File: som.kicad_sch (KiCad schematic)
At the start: 31 parts, among them M1 jetson-orin-nx/nano-module, U4 NTS0102GT

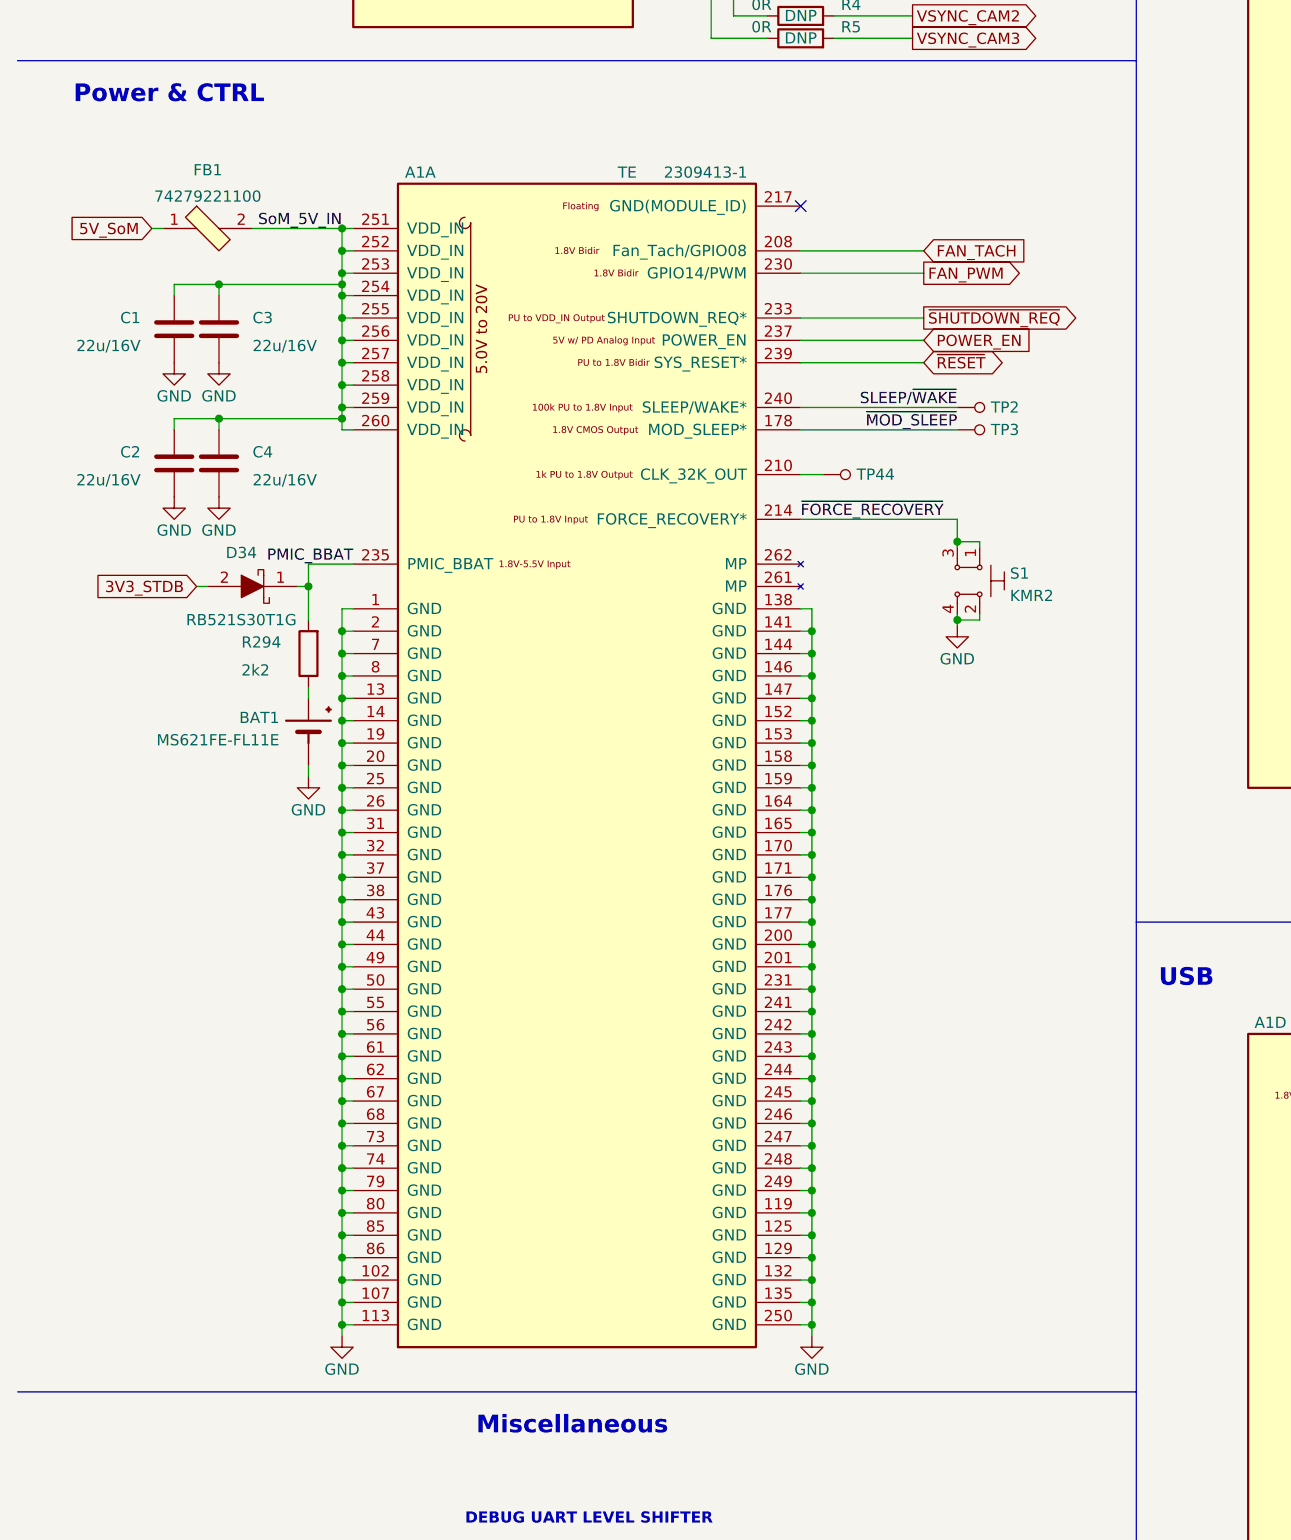
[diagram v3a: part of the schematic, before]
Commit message: Add more capacitors to the SoM VDD_IN
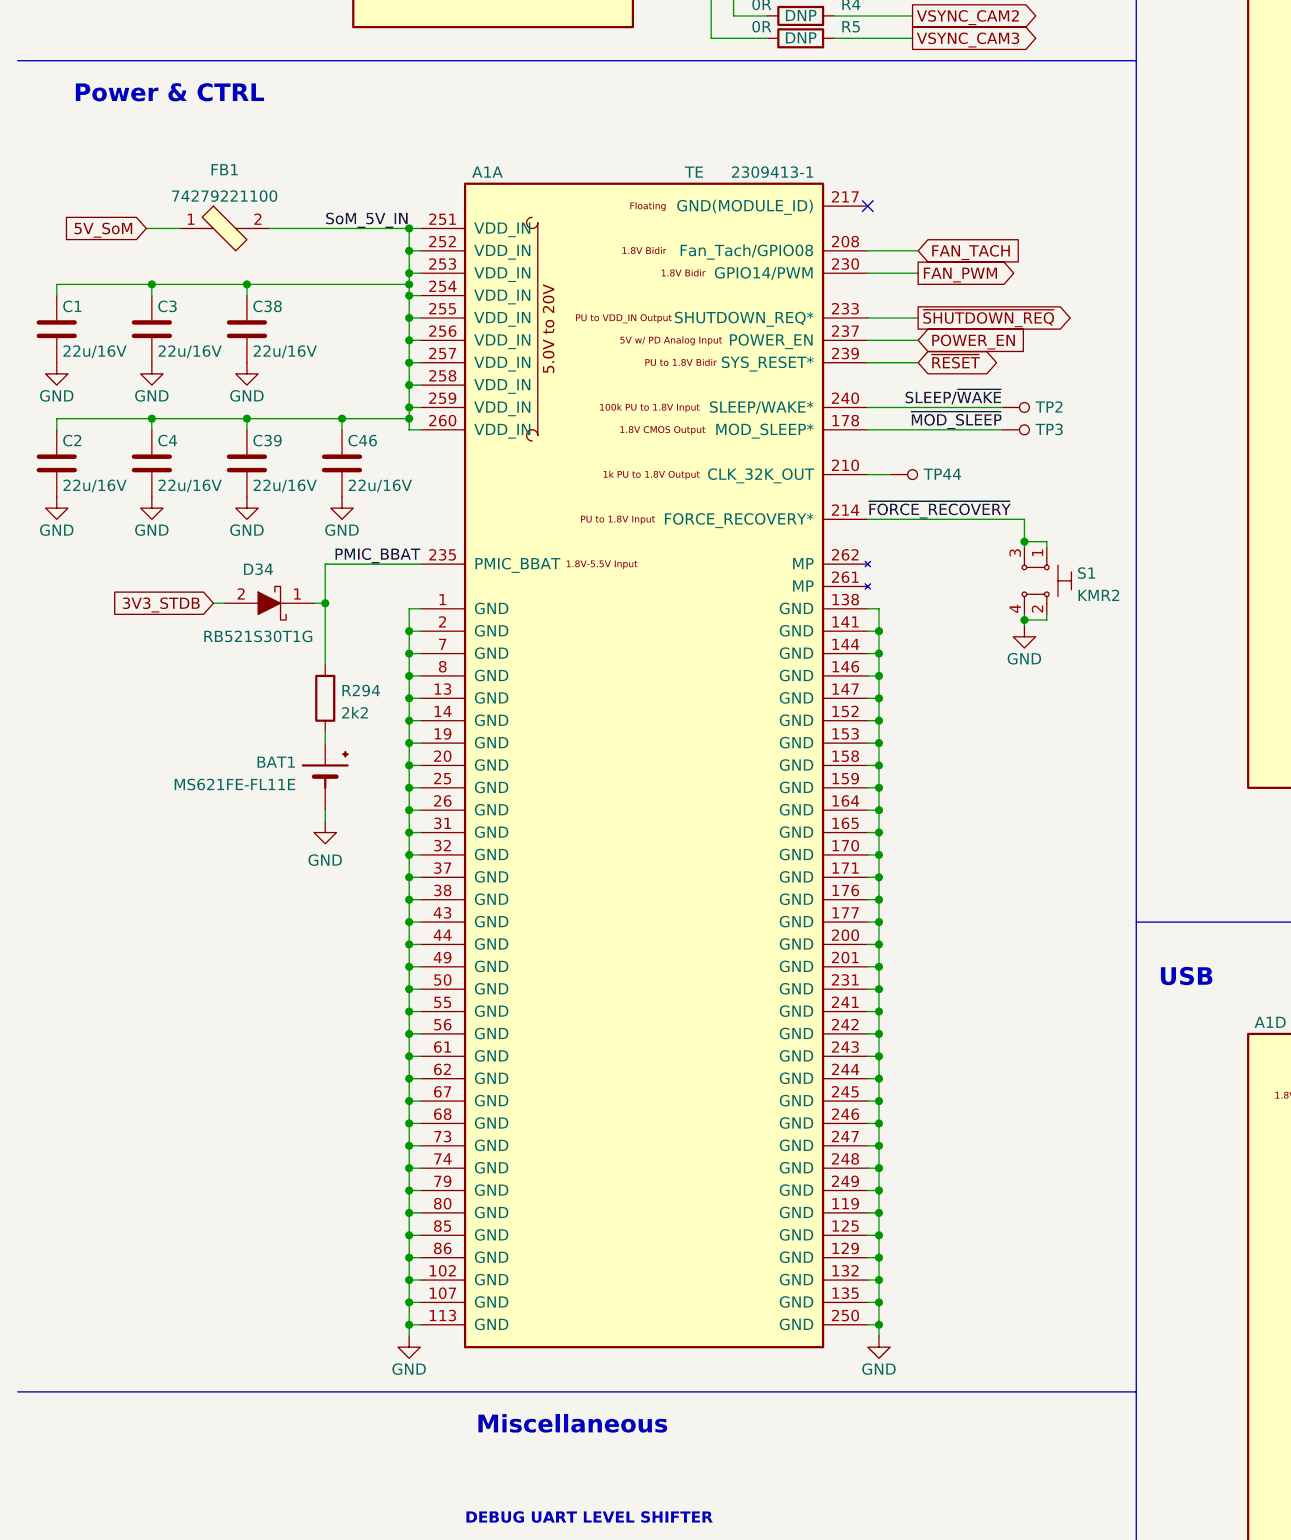
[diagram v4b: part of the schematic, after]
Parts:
- added C38, C39, C46: C_22u_0603_16V, antmicro-footprints:0603-cap, symbol antmicroCapacitors0603:C_22u_0603_16V
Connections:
- net GND: now also C38.2, C39.2, C46.2
- net SoM_5V_IN: now also C38.1, C39.1, C46.1
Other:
- moved on the sheet: A1A, BAT1, C1, C2, C3, C4, D34, FB1, R294, S1, TP2, TP3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

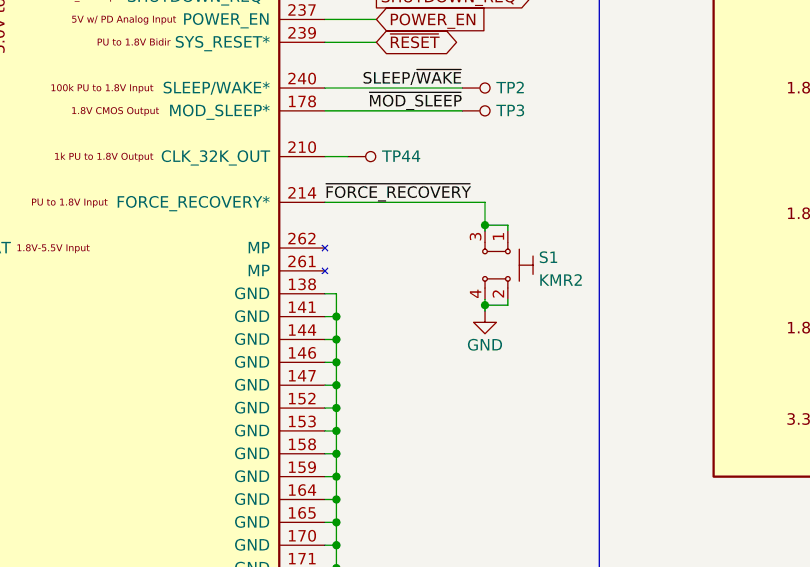
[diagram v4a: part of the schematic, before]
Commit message: Add ESD protection to force recovery button
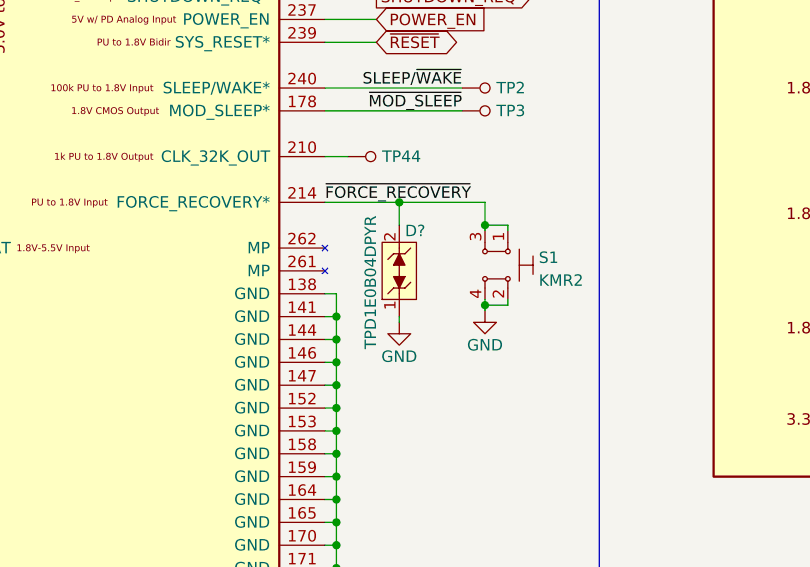
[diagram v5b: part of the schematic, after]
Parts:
- added D?: TPD1E0B04DPYR, jetson-orin-baseboard-footprints:XDFN-2_1x0.60mm, symbol jetson-orin-baseboard:TPD1E0B04DPYR
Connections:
- net GND: now also D?.1
- net ~{FORCE_RECOVERY}: now also D?.2
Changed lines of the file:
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@@
   (junction (at 57.15 165.1) (diameter 0) (color 0 0 0 0)
   )
+  (junction (at 117.475 119.38) (diameter 0) (color 0 0 0 0)
+  )
   (junction (at 57.15 210.82) (diameter 0) (color 0 0 0 0)
   )
@@
     (stroke (width 0) (type default) (color 0 0 0 0))
   )
-  (wire (pts (xy 109.22 119.38) (xy 127 119.38))
+  (wire (pts (xy 109.22 119.38) (xy 117.475 119.38))
     (stroke (width 0) (type default) (color 0 0 0 0))
   )
@@
     (stroke (width 0) (type default) (color 0 0 0 0))
   )
+  (wire (pts (xy 117.475 132.08) (xy 117.475 132.715))
+    (stroke (width 0) (type default) (color 0 0 0 0))
+  )
   (wire (pts (xy 57.15 170.18) (xy 57.15 167.64))
     (stroke (width 0) (type default) (color 0 0 0 0))
@@
     (stroke (width 0) (type default) (color 0 0 0 0))
   )
+  (wire (pts (xy 117.475 119.38) (xy 117.475 121.92))
+    (stroke (width 0) (type default) (color 0 0 0 0))
+  )
   (wire (pts (xy 127 121.92) (xy 127 122.555))
     (stroke (width 0) (type default) (color 0 0 0 0))
@@
     (stroke (width 0) (type default) (color 0 0 0 0))
   )
+  (wire (pts (xy 117.475 119.38) (xy 127 119.38))
+    (stroke (width 0) (type default) (color 0 0 0 0))
+  )
   (wire (pts (xy 109.22 149.86) (xy 110.49 149.86))
     (stroke (width 0) (type default) (color 0 0 0 0))
@@
     (pin "1")
   )
+  (symbol (lib_id "jetson-orin-baseboard:GND") (at 117.475 132.715 0) (unit 1)
+    (in_bom yes) (on_board yes) (fields_autoplaced)
+    (property "Reference" "#PWR?" (id 0) (at 117.475 139.065 0)
+      (effects (font (size 1.27 1.27)) hide)
+    )
+    (property "Value" "GND" (id 1) (at 117.475 136.525 0))
+    (property "Footprint" "" (id 2) (at 117.475 132.715 0)
+      (effects (font (size 1.27 1.27)) hide)
+    )
+    (property "Datasheet" "" (id 3) (at 117.475 132.715 0)
+      (effects (font (size 1.27 1.27)) hide)
+    )
+    (pin "1")
+  )
   (symbol (lib_id "jetson-orin-baseboard:Jetson-Orin-9.2H-socket") (at 184.15 25.4 0) (mirror y) (unit 3)
     (in_bom yes) (on_board yes)
@@
     (pin "8")
   )
+  (symbol (lib_id "jetson-orin-baseboard:TPD1E0B04DPYR ") (at 117.475 127 90) (unit 1)
+    (in_bom yes) (on_board yes)
+    (property "Reference" "D?" (id 0) (at 118.11 122.555 90)
+      (effects (font (size 1.27 1.27)) (justify right))
+    )
+    (property "Value" "TPD1E0B04DPYR " (id 1) (at 114.3 128.27 0))
+    (property "Footprint" "jetson-orin-baseboard-footprints:XDFN-2_1x0.60mm" (id 2) (at 112.395 121.92 0)
+      (effects (font (size 1.524 1.524)) (justify left) hide)
+    )
+    (property "Datasheet" "https://www.ti.com/general/docs/suppproductinfo.tsp?distId=26&gotoUrl=https://www.ti.com/lit/gpn/tpd1e0b04" (id 3) (at 109.855 121.92 0)
+      (effects (font (size 1.524 1.524)) (justify left) hide)
+    )
+    (property "Manufacturer" "Texas Instruments" (id 4) (at 89.535 121.92 0)
+      (effects (font (size 1.524 1.524)) (justify left) hide)
+    )
+    (property "MPN" "TPD1E0B04DPYR " (id 5) (at 104.775 121.92 0)
+      (effects (font (size 1.524 1.524)) (justify left) hide)
+    )
+    (pin "1")
+    (pin "2")
+  )
   (symbol (lib_id "jetson-orin-baseboard:Jetson-Orin-9.2H-socket") (at 82.55 25.4 0) (mirror y) (unit 8)

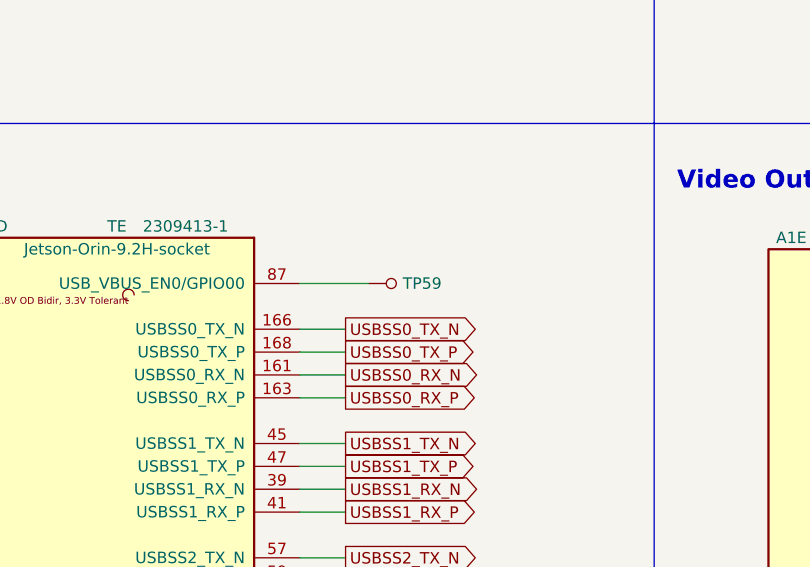
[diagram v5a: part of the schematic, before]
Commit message: Connect USB3 ID detection to GPIO00
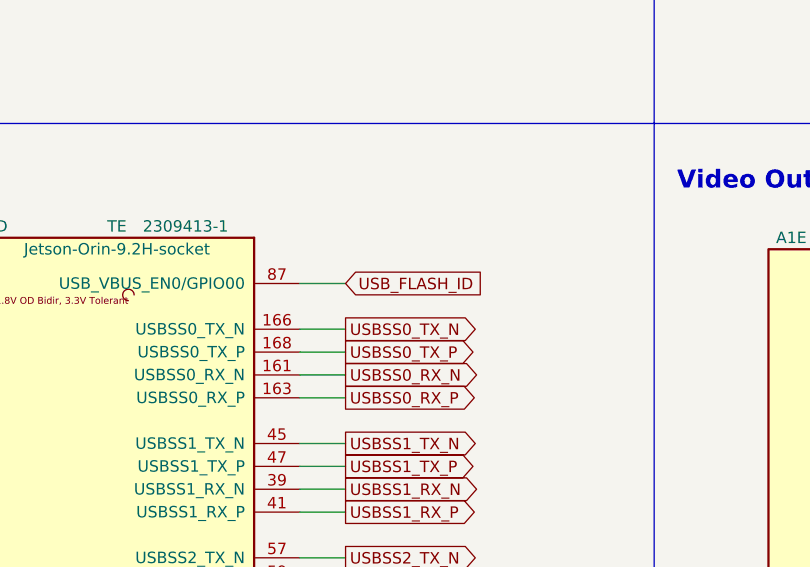
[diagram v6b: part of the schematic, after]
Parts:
- removed TP59: TP_SMD_0_75MM, jetson-orin-baseboard-footprints:Testpoint_smd_0_75mm, symbol jetson-orin-baseboard:TP_SMD_0_75MM
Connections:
- net USB_FLASH_ID: now reaches A1.87 (USB_VBUS_EN0/GPIO00)
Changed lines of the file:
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@@
     (stroke (width 0) (type default) (color 0 0 0 0))
   )
-  (wire (pts (xy 189.23 182.88) (xy 196.85 182.88))
+  (wire (pts (xy 189.23 182.88) (xy 194.31 182.88))
     (stroke (width 0) (type default) (color 0 0 0 0))
   )
@@
     )
   )
+  (global_label "USB_FLASH_ID" (shape input) (at 194.31 182.88 0) (fields_autoplaced)
+    (effects (font (size 1.27 1.27)) (justify left))
+    (property "Intersheet References" "${INTERSHEET_REFS}" (id 0) (at 210.0883 182.8006 0)
+      (effects (font (size 1.27 1.27)) (justify left))
+    )
+  )
   (global_label "POWER_EN" (shape input) (at 114.935 99.06 0)
     (effects (font (size 1.27 1.27)) (justify left))
@@
       (effects (font (size 1.524 1.524)) (justify left) hide)
     )
-    (pin "1")
-  )
-  (symbol (lib_id "jetson-orin-baseboard:TP_SMD_0_75MM") (at 199.39 182.88 90) (unit 1)
-    (in_bom yes) (on_board yes) (fields_autoplaced)
-    (property "Reference" "TP59" (id 0) (at 200.66 182.8799 90)
-      (effects (font (size 1.27 1.27)) (justify right))
-    )
-    (property "Value" "TP_SMD_0_75MM" (id 1) (at 201.93 182.88 0)
-      (effects (font (size 1.27 1.27)) hide)
-    )
-    (property "Footprint" "jetson-orin-baseboard-footprints:Testpoint_smd_0_75mm" (id 2) (at 194.31 177.8 0)
-      (effects (font (size 1.524 1.524)) (justify left) hide)
-    )
-    (property "Datasheet" "" (id 3) (at 191.77 177.8 0)
-      (effects (font (size 1.524 1.524)) (justify left) hide)
-    )

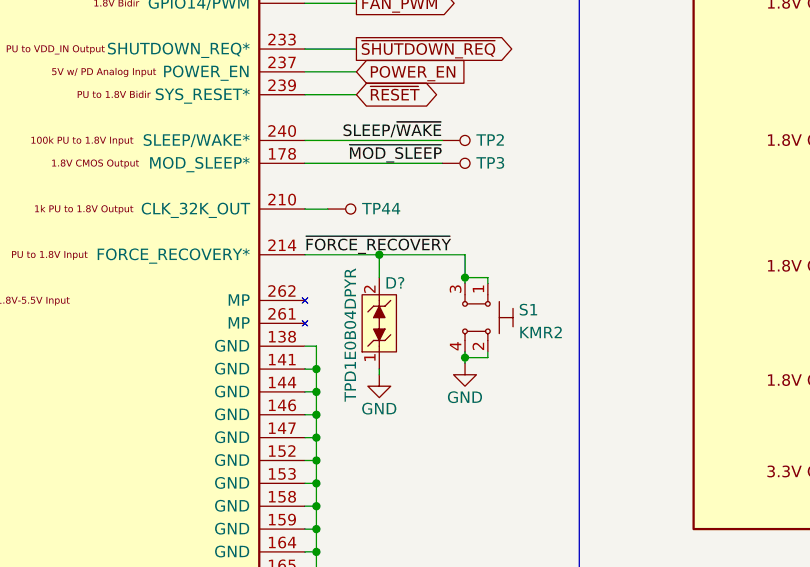
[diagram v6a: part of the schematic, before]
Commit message: Annotate parts, import them on PCB
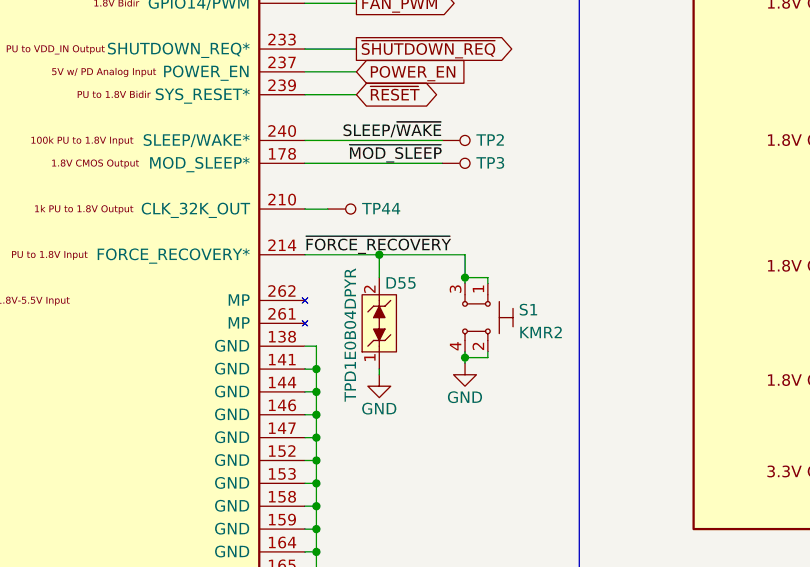
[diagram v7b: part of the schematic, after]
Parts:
- gave numbers to parts that had none: 1
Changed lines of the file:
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@@
   (symbol (lib_id "jetson-orin-baseboard:GND") (at 117.475 132.715 0) (unit 1)
     (in_bom yes) (on_board yes) (fields_autoplaced)
-    (property "Reference" "#PWR?" (id 0) (at 117.475 139.065 0)
+    (property "Reference" "#PWR0112" (id 0) (at 117.475 139.065 0)
       (effects (font (size 1.27 1.27)) hide)
     )
@@
   (symbol (lib_id "jetson-orin-baseboard:TPD1E0B04DPYR ") (at 117.475 127 90) (unit 1)
     (in_bom yes) (on_board yes)
-    (property "Reference" "D?" (id 0) (at 118.11 122.555 90)
+    (property "Reference" "D55" (id 0) (at 118.11 122.555 90)
       (effects (font (size 1.27 1.27)) (justify right))
     )
